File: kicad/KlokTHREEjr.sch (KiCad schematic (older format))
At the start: 25 parts, among them P2 OUT_CLK_DAT, U129 ESP-wroom-32

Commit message: corrected error in pin assignments
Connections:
- net labels added: IO21, NC
- net labels removed: IO16, IO4
- no-connect marks 16 -> 15
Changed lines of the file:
@@
 Text Label 1850 2950 0    40   ~ 0
 LDR1
-Text Label 4050 2950 2    40   ~ 0
+Text Label 4050 3150 2    40   ~ 0
 DAT_IN
 Text Label 1850 2650 0    40   ~ 0
@@
 	4050 2350 3800 2350
 Wire Wire Line
-	4050 2450 3800 2450
-Wire Wire Line
-	3800 2550 4050 2550
-Wire Wire Line
 	4050 2650 3800 2650
 Wire Wire Line
@@
 Wire Wire Line
 	3800 2950 4050 2950
+Wire Wire Line
+	4050 3050 3800 3050
+Wire Wire Line
+	3800 3150 4050 3150
 Wire Wire Line
 	4050 3250 3800 3250
@@
 Text Label 2500 3925 1    40   ~ 0
 GND
-NoConn ~ 3800 3150
 Text Label 4050 1950 2    40   ~ 0
 GND
@@
 Text Label 5450 2000 0    40   ~ 0
 DTR
-Text Label 4050 2850 2    40   ~ 0
+Text Label 4050 3050 2    40   ~ 0
 CLK_IN
 $Comp
@@
 Connection ~ 3150 5725
 Connection ~ 2650 5725
-Text Label 4050 2450 2    40   ~ 0
+Text Label 4050 2650 2    40   ~ 0
 SW_E
-Text Label 4050 2550 2    40   ~ 0
+Text Label 4050 2750 2    40   ~ 0
 SW_I
-Text Label 4050 2650 2    40   ~ 0
+Text Label 4050 2850 2    40   ~ 0
 SW_D
-Text Label 4050 2750 2    40   ~ 0
+Text Label 4050 2950 2    40   ~ 0
 SW_M
 Wire Notes Line
-	4125 2450 4175 2450
-Wire Notes Line
-	4175 2450 4175 2750
-Wire Notes Line
-	4175 2750 4125 2750
-Wire Notes Line
-	4125 2850 4175 2850
-Wire Notes Line
-	4175 2850 4175 2950
+	4125 2650 4175 2650
+Wire Notes Line
+	4175 2650 4175 2950
 Wire Notes Line
 	4175 2950 4125 2950
 Wire Notes Line
+	4125 3050 4175 3050
+Wire Notes Line
+	4175 3050 4175 3150
+Wire Notes Line
+	4175 3150 4125 3150
+Wire Notes Line
 	1750 2450 1700 2450
 Wire Notes Line
@@
 Wire Notes Line
 	1700 2550 1750 2550
-Text Notes 4175 2500 0    40   ~ 0
+Text Notes 4175 2700 0    40   ~ 0
 BUTTONS
-Text Notes 4175 2900 0    40   ~ 0
+Text Notes 4175 3100 0    40   ~ 0
 LED CLK/DAT
 Text Notes 1675 2500 2    40   ~ 0
@@
 NoConn ~ 3800 2050
 NoConn ~ 3800 2150
-NoConn ~ 3800 3050
 NoConn ~ 2100 3250
 Wire Wire Line
@@
 Text Label 3400 3650 3    40   ~ 0
 IO2
-Text Label 3800 3150 0    40   ~ 0
-IO4
-Text Label 3800 3050 0    40   ~ 0
-IO16
 Text Label 3800 2150 0    40   ~ 0
 IO22
 Text Label 3800 2050 0    40   ~ 0
 IO23
+NoConn ~ 3800 2450
+Text Label 3800 2450 0    40   ~ 0
+IO21
+Text Label 3800 2550 0    40   ~ 0
+NC
 $EndSCHEMATC

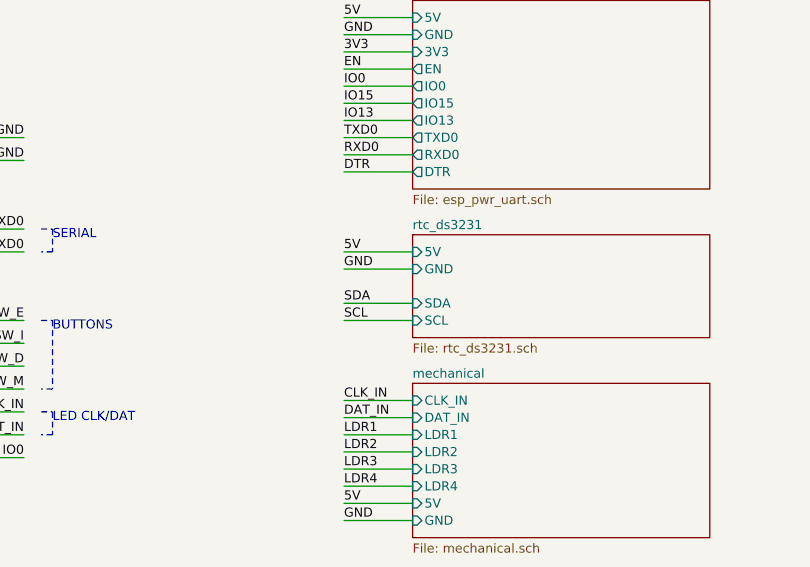
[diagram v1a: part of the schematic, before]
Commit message: added voltage translation ckt for I2C 3V3 to 5V
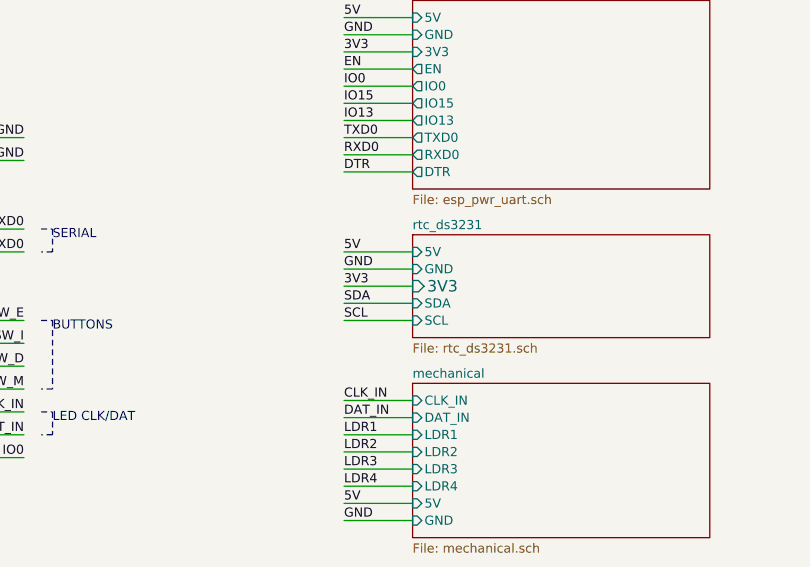
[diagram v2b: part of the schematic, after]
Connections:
- wire segments 229 -> 230
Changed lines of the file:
@@
 F4 "SDA" I L 5750 2575 40
 F5 "SCL" I L 5750 2650 40
+F6 "3V3" I L 5750 2500 50
 $EndSheet
 Wire Wire Line
@@
 Text Label 3800 2550 0    40   ~ 0
 NC
+Wire Wire Line
+	5750 2500 5450 2500
+Text Label 5450 2500 0    40   ~ 0
+3V3
 $EndSCHEMATC

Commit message: removed voltage translation ckt for I2C, added I2C header
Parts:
- added C29, C30, C31: 100nF, KlokTHREEjr_libs:c_0805, symbol KlokTHREEjr:C_NP
- added J17: MISO, KlokTHREEjr_libs:BreakOutPad, symbol KlokTHREEjr:Conn_01x01
- added J18: 3V3, KlokTHREEjr_libs:BreakOutPad, symbol KlokTHREEjr:Conn_01x01
- added J19: SCK, KlokTHREEjr_libs:BreakOutPad, symbol KlokTHREEjr:Conn_01x01
- added J20: SPI, KlokTHREEjr_libs:Header_ISP, symbol KlokTHREEjr:Conn_02x03_Odd_Even
- added J21: MOSI, KlokTHREEjr_libs:BreakOutPad, symbol KlokTHREEjr:Conn_01x01
- added J22: RST, KlokTHREEjr_libs:BreakOutPad, symbol KlokTHREEjr:Conn_01x01
- added J23: GND, KlokTHREEjr_libs:BreakOutPad, symbol KlokTHREEjr:Conn_01x01
- added J24: I2C_ext1, KlokTHREEjr_libs:Header_4x1, symbol KlokTHREEjr:Conn_01x04
- added J25: I2C_ext2, KlokTHREEjr_libs:Header_4x1, symbol KlokTHREEjr:Conn_01x04
- P2: symbol KlokTHREEjr:CONN_2 -> KlokTHREEjr:Conn_01x02
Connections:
- net labels added: MISO, MOSI, RST, SCK
- wire segments 230 -> 255
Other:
- note added: "I2C HEADER"
- note added: "I2C interface for external\nconnections to sensors etc.\n"
- note added: "Native SPI pins are (clk, mosi, miso, cs):\nSPI1: 6, 8, 7, 11\nHSPI: 14,13,12,15\nVSPI: 18,23,19, 5\nIf using native pins maximum \nSPI clock can be set to 80 MHZ.\nOnly HSPI & VSPI are supported by esp-idf driver."
- note added: "SPI HEADER"
- note added: "SPI header with breakour pins.\nConnect with wire to appropriate\npins on ESP32"

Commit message: added I2C and SPI headers
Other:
- note added: "Native SPI pins are (clk, mosi, miso, cs):\nSPI1: 6, 8, 7, 11\nHSPI: 14,13,12,15\nVSPI: 18,23,19, 5\nIf using native pins max SPI clock can be set to 80 MHZ.\nOnly HSPI & VSPI are supported by esp-idf driver."
- note added: "SPI header with breakout pins.\nConnect with wire to appropriate\npins on ESP32"
- note removed: "Native SPI pins are (clk, mosi, miso, cs):\nSPI1: 6, 8, 7, 11\nHSPI: 14,13,12,15\nVSPI: 18,23,19, 5\nIf using native pins maximum \nSPI clock can be set to 80 MHZ.\nOnly HSPI & VSPI are supported by esp-idf driver."
- note removed: "SPI header with breakour pins.\nConnect with wire to appropriate\npins on ESP32"
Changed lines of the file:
@@
 Text Label 5425 1975 0    40   ~ 0
 3V3
-Text Notes 2275 5100 0    40   ~ 0
-Native SPI pins are (clk, mosi, miso, cs):\nSPI1: 6, 8, 7, 11\nHSPI: 14,13,12,15\nVSPI: 18,23,19, 5\nIf using native pins maximum \nSPI clock can be set to 80 MHZ.\nOnly HSPI & VSPI are supported by esp-idf driver.
+Text Notes 2200 5350 0    40   ~ 0
+Native SPI pins are (clk, mosi, miso, cs):\nSPI1: 6, 8, 7, 11\nHSPI: 14,13,12,15\nVSPI: 18,23,19, 5\nIf using native pins max SPI clock can be set to 80 MHZ.\nOnly HSPI & VSPI are supported by esp-idf driver.
 $Comp
 L KlokTHREEjr:Conn_02x03_Odd_Even J20
@@
 	1    0    0    -1
 $EndComp
-Text Notes 2275 5375 0    40   ~ 0
-SPI header with breakour pins.\nConnect with wire to appropriate\npins on ESP32
+Text Notes 2200 4900 0    40   ~ 0
+SPI header with breakout pins.\nConnect with wire to appropriate\npins on ESP32
 Wire Notes Line
 	5375 3325 7375 3325

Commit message: K3jr schematic modified
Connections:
- net labels added: IO34, IO35
- net labels removed: IO21, IO22
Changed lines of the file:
@@
 Text Notes 8175 550  0    40   ~ 8
 16 x 8 pixel matrix
-Text Label 1825 1925 0    40   ~ 0
+Text Label 4025 1625 2    40   ~ 0
 SCL
-Text Label 1825 2025 0    40   ~ 0
+Text Label 4025 1925 2    40   ~ 0
 SDA
 Text Label 8400 1300 0    40   ~ 0
@@
 	1825 2425 2075 2425
 Wire Wire Line
-	2075 1925 1825 1925
-Wire Wire Line
-	1825 2025 2075 2025
-Wire Wire Line
 	4025 1425 3775 1425
 Wire Wire Line
@@
 Wire Notes Line
 	4150 2625 4100 2625
-Wire Notes Line
-	1725 1925 1675 1925
-Wire Notes Line
-	1675 1925 1675 2025
-Wire Notes Line
-	1675 2025 1725 2025
 Text Notes 4150 2175 0    40   ~ 0
 BUTTONS
 Text Notes 4150 2575 0    40   ~ 0
 LED CLK/DAT
-Text Notes 1650 1975 2    40   ~ 0
+Text Notes 4500 1675 2    40   ~ 0
 I2C
 Wire Notes Line
@@
 NoConn ~ 2675 3125
 NoConn ~ 3775 1525
-NoConn ~ 3775 1625
+NoConn ~ 2075 1925
 Wire Wire Line
 	3775 1325 4025 1325
@@
 Text Label 3375 3125 3    40   ~ 0
 IO2
-Text Label 3775 1625 0    40   ~ 0
-IO22
 Text Label 3775 1525 0    40   ~ 0
 IO23
-NoConn ~ 3775 1925
-Text Label 3775 1925 0    40   ~ 0
-IO21
+NoConn ~ 2075 2025
 Text Label 3775 2025 0    40   ~ 0
 NC
@@
 	1    0    0    -1
 $EndComp
+Text Label 2425 5900 0    40   ~ 0
+SDA
 Text Label 2425 5800 0    40   ~ 0
-SDA
-Text Label 2425 5900 0    40   ~ 0
 SCL
 Text Label 2425 6000 0    40   ~ 0
@@
 	1    0    0    -1
 $EndComp
+Text Label 3475 5900 0    40   ~ 0
+SDA
 Text Label 3475 5800 0    40   ~ 0
-SDA
-Text Label 3475 5900 0    40   ~ 0
 SCL
 Text Label 3475 6000 0    40   ~ 0
@@
 Wire Wire Line
 	3400 4350 3625 4350
+Text Label 2075 1925 2    40   ~ 0
+IO34
+Text Label 2075 2025 2    40   ~ 0
+IO35
+Wire Wire Line
+	4025 1625 3775 1625
+Wire Wire Line
+	3775 1925 4025 1925
+Wire Notes Line
+	4100 1625 4375 1625
+Wire Notes Line
+	4375 1625 4375 1925
+Wire Notes Line
+	4375 1925 4100 1925
 $EndSCHEMATC

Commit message: USB protection, LDR, Switches reconfigured
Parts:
- removed LDR3, LDR4: LDR, KlokTHREEjr_libs:r_0805_ldr, symbol KlokTHREEjr:LDR03
- removed R14, R15: 10k, KlokTHREEjr_libs:r_0805, symbol KlokTHREEjr:R
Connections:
- net labels added: IO25, IO26
- net labels removed: LDR3, LDR4
- wire segments 255 -> 235
- no-connect marks 15 -> 17
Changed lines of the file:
@@
 Text Label 8325 650  0    40   ~ 0
 DAT_IN
-Text Label 1825 2425 0    40   ~ 0
-LDR1
 Text Label 4025 2625 2    40   ~ 0
 DAT_IN
+Text Label 1825 2225 0    40   ~ 0
+LDR1
 Text Label 1825 2125 0    40   ~ 0
 LDR2
-Text Label 1825 2225 0    40   ~ 0
-LDR3
 Text Label 8475 1850 0    40   ~ 0
 5V
@@
 	1    0    0    -1
 $EndComp
-Text Label 5675 5725 0    40   ~ 0
+Text Label 5825 5725 2    40   ~ 0
 LDR1
-Text Label 5575 5125 0    40   ~ 0
-5V
 Text Label 5575 6325 0    40   ~ 0
 GND
@@
 	5575 6150 5575 6325
 Wire Wire Line
-	5575 5725 5675 5725
+	5575 5725 5825 5725
 Connection ~ 5575 5725
 Wire Wire Line
@@
 	1    0    0    -1
 $EndComp
-Text Label 6175 5725 0    40   ~ 0
+Text Label 6325 5725 2    40   ~ 0
 LDR2
 Wire Wire Line
@@
 	6075 6325 6075 6150
 Wire Wire Line
-	6075 5725 6175 5725
+	6075 5725 6325 5725
 Connection ~ 6075 5725
 Text Notes 5400 5000 0    40   ~ 8
 Light sensors (LDR)
-$Comp
-L KlokTHREEjr:R R14
-U 1 1 54C1D9CF
-P 6575 6000
-F 0 "R14" H 6650 5850 40  0000 C CNN
-F 1 "10k" V 6582 6001 40  0000 C CNN
-F 2 "KlokTHREEjr_libs:r_0805" V 6505 6000 30  0001 C CNN
-F 3 "" H 6575 6000 30  0000 C CNN
-	1    6575 6000
-	1    0    0    -1
-$EndComp
-Text Label 6675 5725 0    40   ~ 0
-LDR3
-Wire Wire Line
-	6575 5125 6575 5275
-Wire Wire Line
-	6575 5575 6575 5725
-Wire Wire Line
-	6575 6325 6575 6150
-Wire Wire Line
-	6575 5725 6675 5725
-Connection ~ 6575 5725
-$Comp
-L KlokTHREEjr:R R15
-U 1 1 56100223
-P 7075 6000
-F 0 "R15" H 7150 5850 40  0000 C CNN
-F 1 "10k" V 7082 6001 40  0000 C CNN
-F 2 "KlokTHREEjr_libs:r_0805" V 7005 6000 30  0001 C CNN
-F 3 "" H 7075 6000 30  0000 C CNN
-	1    7075 6000
-	1    0    0    -1
-$EndComp
-Text Label 7175 5725 0    40   ~ 0
-LDR4
-Wire Wire Line
-	7075 5125 7075 5275
-Wire Wire Line
-	7075 5575 7075 5725
-Wire Wire Line
-	7075 6325 7075 6150
-Wire Wire Line
-	7075 5725 7175 5725
-Connection ~ 7075 5725
-Text Label 1825 2325 0    40   ~ 0
-LDR4
 $Comp
 L KlokTHREEjr:ESP-wroom-32 U129
@@
 F2 "CLK_IN" I L 5725 2475 40
 F3 "DAT_IN" I L 5725 2550 40
-F4 "LDR1" I L 5725 2625 40
-F5 "LDR2" I L 5725 2700 40
-F6 "LDR4" I L 5725 2850 40
-F7 "LDR3" I L 5725 2775 40
-F8 "5V" I L 5725 2925 40
-F9 "GND" I L 5725 3000 40
+F4 "5V" I L 5725 2925 40
+F5 "GND" I L 5725 3000 40
 $EndSheet
 $Sheet
@@
 	1825 2225 2075 2225
 Wire Wire Line
-	2075 2325 1825 2325
-Wire Wire Line
-	1825 2425 2075 2425
-Wire Wire Line
 	4025 1425 3775 1425
 Wire Wire Line
@@
 F 3 "" H 6075 5375 50  0000 C CNN
 	1    6075 5425
-	1    0    0    -1
-$EndComp
-$Comp
-L KlokTHREEjr:LDR03 LDR3
-U 1 1 5A635AFD
-P 6575 5425
-F 0 "LDR3" H 6600 5275 40  0000 L CNN
-F 1 "LDR" V 6575 5375 40  0000 L CNN
-F 2 "KlokTHREEjr_libs:r_0805_ldr" V 6750 5425 50  0001 C CNN
-F 3 "" H 6575 5375 50  0000 C CNN
-	1    6575 5425
-	1    0    0    -1
-$EndComp
-$Comp
-L KlokTHREEjr:LDR03 LDR4
-U 1 1 5A635C9D
-P 7075 5425
-F 0 "LDR4" H 7100 5275 40  0000 L CNN
-F 1 "LDR" V 7075 5375 40  0000 L CNN
-F 2 "KlokTHREEjr_libs:r_0805_ldr" V 7250 5425 50  0001 C CNN
-F 3 "" H 7075 5375 50  0000 C CNN
-	1    7075 5425
 	1    0    0    -1
 $EndComp
@@
 Text Label 6225 4175 2    40   ~ 0
 SW_I
-Text Label 5550 3525 0    40   ~ 0
-5V
 Wire Wire Line
 	5525 4025 5525 4050
@@
 SERIAL
 Wire Notes Line
-	1725 2425 1675 2425
-Wire Notes Line
-	1675 2425 1675 2125
+	1725 2225 1675 2225
 Wire Notes Line
 	1675 2125 1725 2125
 Text Notes 1650 2175 2    40   ~ 0
 LDR
-Connection ~ 6075 5125
-Connection ~ 6575 5125
-Connection ~ 6575 6325
-Connection ~ 6075 6325
 $Comp
 L KlokTHREEjr:C_POL C27
@@
 	6075 5725 6075 5850
 Wire Wire Line
-	6575 5725 6575 5850
-Wire Wire Line
-	7075 5725 7075 5850
-Wire Wire Line
 	6525 4050 6525 4175
 Wire Wire Line
@@
 	6025 4725 6525 4725
 Wire Wire Line
-	6075 5125 6575 5125
-Wire Wire Line
-	6575 5125 7075 5125
-Wire Wire Line
-	6575 6325 7075 6325
-Wire Wire Line
-	6075 6325 6575 6325
-Wire Wire Line
 	1075 1525 2075 1525
 Wire Wire Line
@@
 Wire Wire Line
 	5425 2550 5725 2550
-Wire Wire Line
-	5725 2625 5425 2625
-Wire Wire Line
-	5425 2700 5725 2700
-Wire Wire Line
-	5725 2775 5425 2775
-Wire Wire Line
-	5425 2850 5725 2850
 Wire Wire Line
 	5725 2925 5425 2925
@@
 Text Label 5425 2550 0    40   ~ 0
 DAT_IN
-Text Label 5425 2625 0    40   ~ 0
-LDR1
-Text Label 5425 2700 0    40   ~ 0
-LDR2
-Text Label 5425 2775 0    40   ~ 0
-LDR3
-Text Label 5425 2850 0    40   ~ 0
-LDR4
 Text Label 5425 2925 0    40   ~ 0
 5V
@@
 Wire Notes Line
 	4375 1925 4100 1925
+Text Label 5525 3525 0    40   ~ 0
+3V3
+Text Label 5575 5125 0    40   ~ 0
+3V3
+Wire Notes Line
+	1675 2125 1675 2225
+NoConn ~ 2075 2325
+NoConn ~ 2075 2425
+Text Label 2075 2325 2    40   ~ 0
+IO25
+Text Label 2075 2425 2    40   ~ 0
+IO26
 $EndSCHEMATC

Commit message: ready for seeed submission
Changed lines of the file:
@@
 Connection ~ 6525 4725
 Connection ~ 6025 4725
+Text Label 4025 2425 2    40   ~ 0
+SW_E
+Text Label 4025 2325 2    40   ~ 0
+SW_I
+Text Label 4025 2225 2    40   ~ 0
+SW_D
 Text Label 4025 2125 2    40   ~ 0
-SW_E
-Text Label 4025 2225 2    40   ~ 0
-SW_I
-Text Label 4025 2325 2    40   ~ 0
-SW_D
-Text Label 4025 2425 2    40   ~ 0
 SW_M
 Wire Notes Line

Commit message: moved APA102 to DNP row on BoM
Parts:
- LDR1, LDR2: footprint KlokTHREEjr_libs:r_0805_ldr -> KlokTHREEjr_libs:r_0805_ldr_2
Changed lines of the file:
@@
 F 0 "LDR1" H 5600 5275 40  0000 L CNN
 F 1 "LDR" V 5575 5375 40  0000 L CNN
-F 2 "KlokTHREEjr_libs:r_0805_ldr" V 5750 5425 50  0001 C CNN
+F 2 "KlokTHREEjr_libs:r_0805_ldr_2" V 5750 5425 50  0001 C CNN
 F 3 "" H 5575 5375 50  0000 C CNN
 	1    5575 5425
@@
 F 0 "LDR2" H 6100 5275 40  0000 L CNN
 F 1 "LDR" V 6075 5375 40  0000 L CNN
-F 2 "KlokTHREEjr_libs:r_0805_ldr" V 6250 5425 50  0001 C CNN
+F 2 "KlokTHREEjr_libs:r_0805_ldr_2" V 6250 5425 50  0001 C CNN
 F 3 "" H 6075 5375 50  0000 C CNN
 	1    6075 5425
